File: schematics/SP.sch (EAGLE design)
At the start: 21 parts

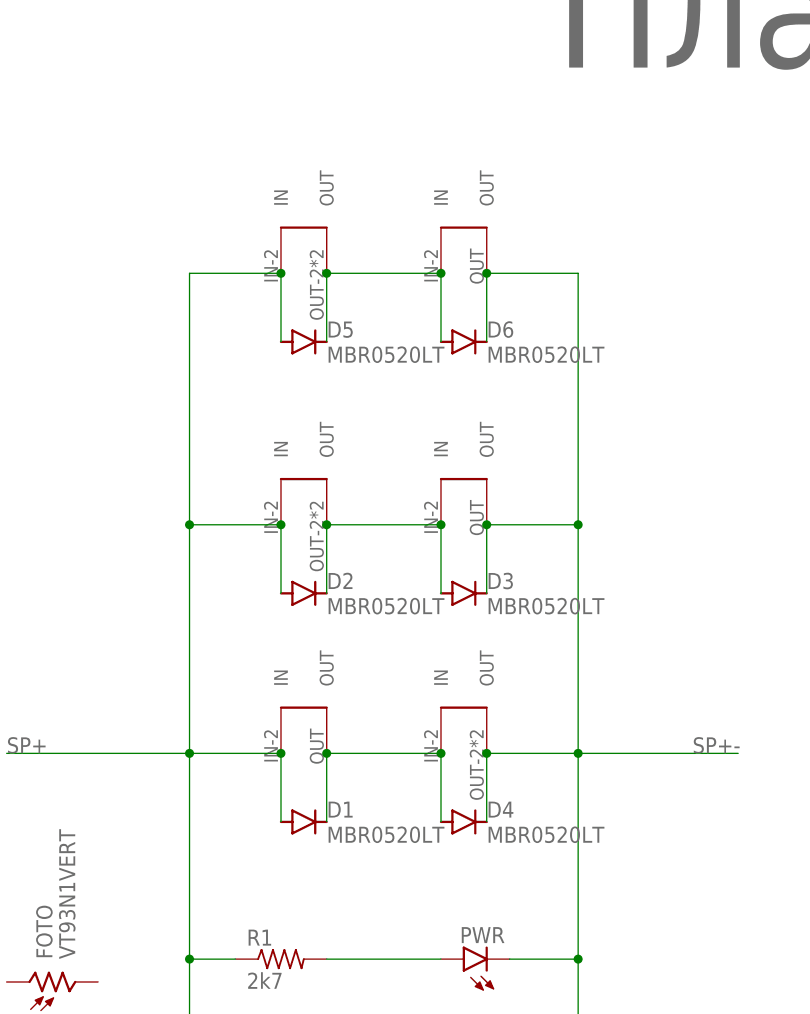
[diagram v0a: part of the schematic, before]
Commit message: схема платы моторов исправлена
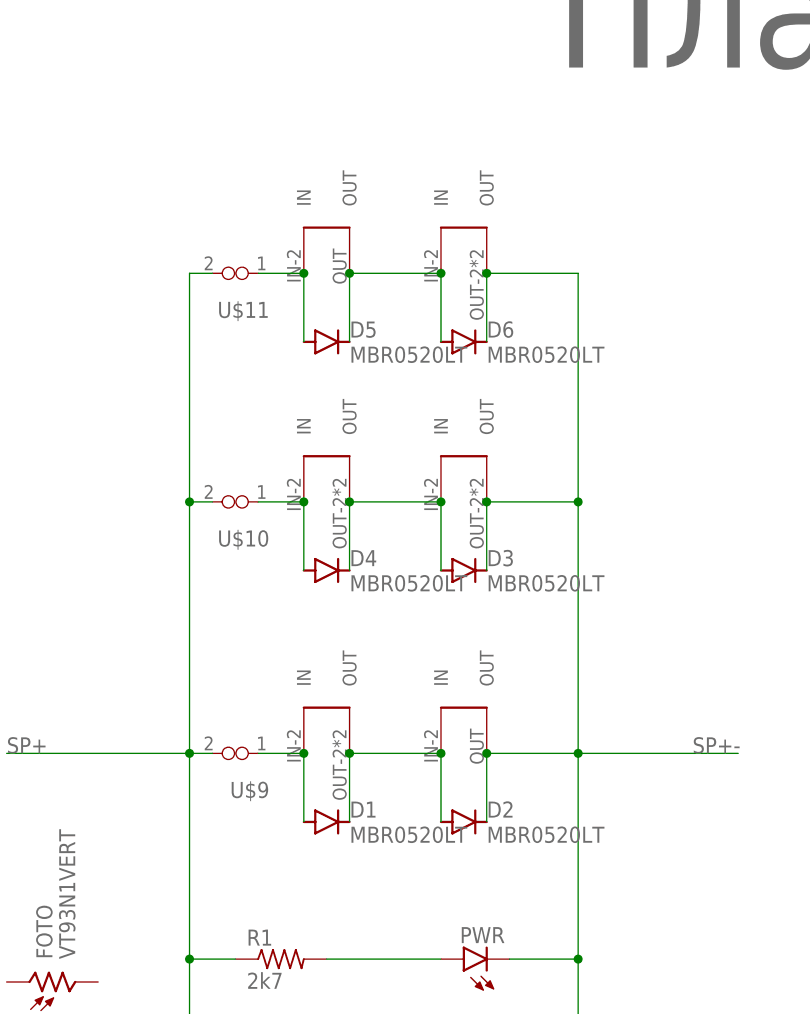
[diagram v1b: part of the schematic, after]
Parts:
- added U$10, U$11, U$9: (no value), KNPN-2023:VIAS-CONNECT
- U$1, U$3, U$8: value SOLAR-2_1 -> SOLAR-2_INVERT0-2; device KNPN-2023:SOLAR-2_1 -> KNPN-2023:SOLAR-2_INVERT0-2
- U$2, U$6: value SOLAR-2_0 -> SOLAR-2_INVERT1-2; device KNPN-2023:SOLAR-2_0 -> KNPN-2023:SOLAR-2_INVERT1-2
- U$4: value SOLAR-2_0 -> SOLAR-2_INVERT0-2; device KNPN-2023:SOLAR-2_0 -> KNPN-2023:SOLAR-2_INVERT0-2
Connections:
- new net N$5: D1.C, D2.A, U$1.OUT, U$2.IN
- new net N$6: D3.A, D4.C, U$3.IN, U$4.OUT
- new net N$7: D1.A, U$1.IN, U$9.1
- net N$2: now also D5.A, U$11.1, U$6.IN; no longer D2.C, D3.A, U$2.OUT, U$3.IN
- net N$3: now also U$10.1; no longer D1.C, U$1.OUT
- net SP+: now also U$10.2, U$11.2, U$9.2; no longer D1.A, D2.A, D5.A, U$1.IN, U$2.IN, U$6.IN
- net SP+-: now also D2.C, U$2.OUT; no longer D4.C, U$4.OUT
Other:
- moved on the sheet: D1, D2, D3, D4, D5
